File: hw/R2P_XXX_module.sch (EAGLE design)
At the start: 32 parts, among them U1 STM32F103CX, U5 LD3985XX, X1 MICROMATCH-6

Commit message: Board layout completed
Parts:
- JP1, JP2: device pinhead:PINHD-1X4 -> misc:PINHD-1X4
- X1: value MICROMATCH-6 -> MICROMATCH-4; device con-amp-micromatch:MICROMATCH-6 -> con-amp-micromatch:MICROMATCH-4
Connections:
- net UART_RX: now also X1-4.S
- net UART_TX: now also X1-3.S
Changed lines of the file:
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@@
 <setting verticaltext="up"/>
 </settings>
-<grid distance="0.1" unitdist="inch" unit="inch" style="lines" multiple="1" display="no" altdistance="0.01" altunitdist="inch" altunit="inch"/>
+<grid distance="0.1" unitdist="inch" unit="inch" style="lines" multiple="1" display="yes" altdistance="0.01" altunitdist="inch" altunit="inch"/>
 <layers>
 <layer number="1" name="Top" color="4" fill="1" visible="no" active="no"/>
@@
 <part name="FRAME2" library="frames" deviceset="DINA3_L" device=""/>
 <part name="1" library="molex" deviceset="RJ45-43860" device=""/>
-<part name="JP1" library="pinhead" deviceset="PINHD-1X4" device=""/>
+<part name="JP1" library="misc" deviceset="PINHD-1X4" device=""/>
 <part name="GND1" library="supply1" deviceset="GND" device=""/>
 <part name="2" library="molex" deviceset="RJ45-43860" device=""/>
-<part name="JP2" library="pinhead" deviceset="PINHD-1X4" device=""/>
+<part name="JP2" library="misc" deviceset="PINHD-1X4" device=""/>
 <part name="GND19" library="supply1" deviceset="GND" device=""/>
 <part name="U$1" library="crystal" deviceset="ASE" device=""/>
 <part name="+3V5" library="supply1" deviceset="+3V3" device=""/>
-<part name="X1" library="con-amp-micromatch" deviceset="MICROMATCH-6" device=""/>
 <part name="R2" library="rcl" deviceset="R-EU_" device="R0603" value="10k"/>
 <part name="GND7" library="supply1" deviceset="GND" device=""/>
@@
 <part name="C1" library="rcl" deviceset="C-EU" device="C0603" value="100n"/>
 <part name="GND9" library="supply1" deviceset="GND" device=""/>
+<part name="X1" library="con-amp-micromatch" deviceset="MICROMATCH-4" device=""/>
 </parts>
 <sheets>
@@
 <instance part="U$1" gate="G$1" x="116.84" y="175.26"/>
 <instance part="+3V5" gate="G$1" x="93.98" y="185.42"/>
-<instance part="X1" gate="-1" x="205.74" y="76.2"/>
-<instance part="X1" gate="-2" x="205.74" y="73.66"/>
-<instance part="X1" gate="-3" x="205.74" y="71.12"/>
-<instance part="X1" gate="-4" x="205.74" y="68.58"/>
-<instance part="X1" gate="-5" x="205.74" y="66.04"/>
-<instance part="X1" gate="-6" x="205.74" y="63.5"/>
 <instance part="R2" gate="G$1" x="129.54" y="208.28" rot="R90"/>
 <instance part="GND7" gate="1" x="129.54" y="198.12"/>
@@
 <instance part="C1" gate="G$1" x="99.06" y="238.76"/>
 <instance part="GND9" gate="1" x="99.06" y="231.14"/>
+<instance part="X1" gate="-1" x="205.74" y="76.2"/>
+<instance part="X1" gate="-2" x="205.74" y="73.66"/>
+<instance part="X1" gate="-3" x="205.74" y="71.12"/>
+<instance part="X1" gate="-4" x="205.74" y="68.58"/>
 </instances>
 <busses>
@@
 </segment>
 <segment>
-<pinref part="X1" gate="-2" pin="S"/>
 <wire x1="210.82" y1="73.66" x2="231.14" y2="73.66" width="0.1524" layer="91"/>
 <pinref part="GND8" gate="1" pin="GND"/>
+<pinref part="X1" gate="-2" pin="S"/>
 </segment>
 <segment>
@@
 <label x="17.78" y="38.1" size="1.778" layer="95"/>
 </segment>
+<segment>
+<pinref part="X1" gate="-3" pin="S"/>
+<wire x1="210.82" y1="71.12" x2="215.9" y2="71.12" width="0.1524" layer="91"/>
+<label x="215.9" y="71.12" size="1.778" layer="95"/>
+</segment>
 </net>
 <net name="UART_RX" class="0">
@@
 <wire x1="33.02" y1="10.16" x2="27.94" y2="10.16" width="0.1524" layer="91"/>
 <label x="17.78" y="10.16" size="1.778" layer="95"/>
+</segment>
+<segment>
+<pinref part="X1" gate="-4" pin="S"/>
+<wire x1="210.82" y1="68.58" x2="215.9" y2="68.58" width="0.1524" layer="91"/>
+<label x="215.9" y="68.58" size="1.778" layer="95"/>
 </segment>
 </net>
@@
 <net name="+5V" class="0">
 <segment>
-<pinref part="X1" gate="-1" pin="S"/>
 <wire x1="210.82" y1="76.2" x2="218.44" y2="76.2" width="0.1524" layer="91"/>
 <wire x1="218.44" y1="76.2" x2="218.44" y2="81.28" width="0.1524" layer="91"/>
 <pinref part="P+5" gate="1" pin="+5V"/>
-</segment>
-<segment>
+<pinref part="X1" gate="-1" pin="S"/>
+</segment>
+<segment>

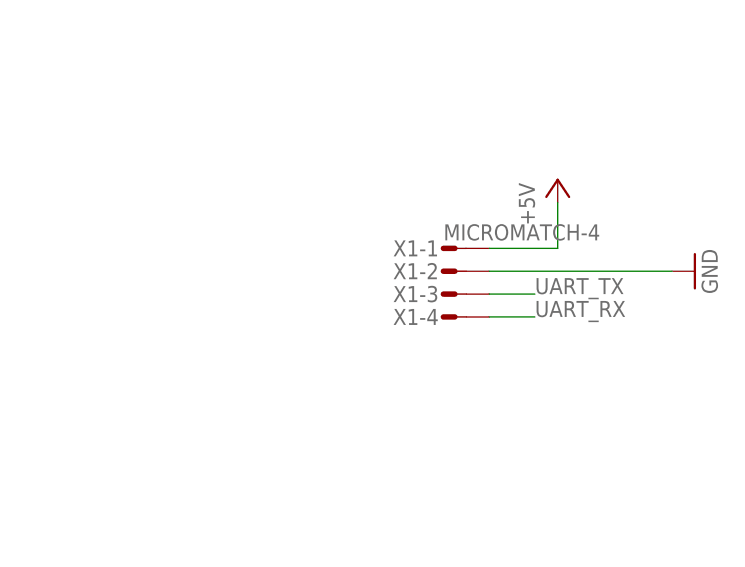
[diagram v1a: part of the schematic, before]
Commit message: Updated micromatch connector
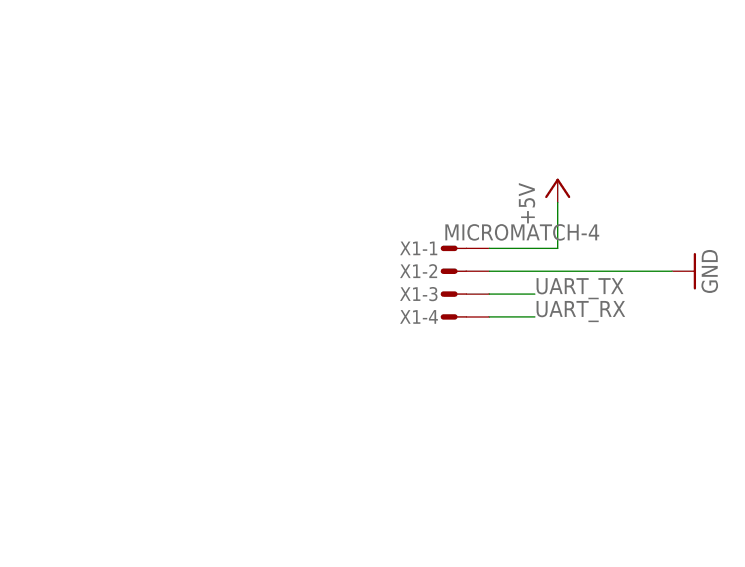
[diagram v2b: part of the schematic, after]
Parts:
- X1: device con-amp-micromatch:MICROMATCH-4 -> tyco:MICROMATCH-4
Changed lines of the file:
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@@
 <setting verticaltext="up"/>
 </settings>
-<grid distance="0.1" unitdist="inch" unit="inch" style="lines" multiple="1" display="yes" altdistance="0.01" altunitdist="inch" altunit="inch"/>
+<grid distance="0.1" unitdist="inch" unit="inch" style="lines" multiple="1" display="no" altdistance="0.01" altunitdist="inch" altunit="inch"/>
 <layers>
 <layer number="1" name="Top" color="4" fill="1" visible="no" active="no"/>
@@
 <part name="C1" library="rcl" deviceset="C-EU" device="C0603" value="100n"/>
 <part name="GND9" library="supply1" deviceset="GND" device=""/>
-<part name="X1" library="con-amp-micromatch" deviceset="MICROMATCH-4" device=""/>
+<part name="X1" library="tyco" deviceset="MICROMATCH-4" device=""/>
 </parts>
 <sheets>
